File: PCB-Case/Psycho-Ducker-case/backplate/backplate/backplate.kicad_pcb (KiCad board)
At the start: 2 copper layers, 310.6 x 124.2 mm, 0 parts

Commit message: fix: backplate filling
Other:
- board size 310.6 x 124.2 mm -> 310 x 124 mm

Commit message: feat: backplate now has mounting holes compatible with the main pcb
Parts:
- added G***: LOGO, LOGO, F.Cu at (215.0, 141.0)
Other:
- outline, holes or cut-outs redrawn

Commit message: feat: changed backplate pattern
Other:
- outline, holes or cut-outs redrawn
- board text added: "NB: to be flipped, the holes are in reference to the front of the pcb"

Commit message: feat: added rubber feet placement
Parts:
- added G***: LOGO, LOGO, B.Cu at (200.0, 139.0)
- G***: moved to B.Cu
- moved G*** 2.00 mm to (215.0, 143.0), turned to 180 degrees
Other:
- outline, holes or cut-outs redrawn
- board text removed: "NB: to be flipped, the holes are in reference to the front of the pcb"

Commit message: feat: added _style_ to the pcb
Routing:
- net (no net): track 0.00 -> 8970.7 mm
- added copper zone on F.Cu, net (none)
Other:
- outline, holes or cut-outs redrawn

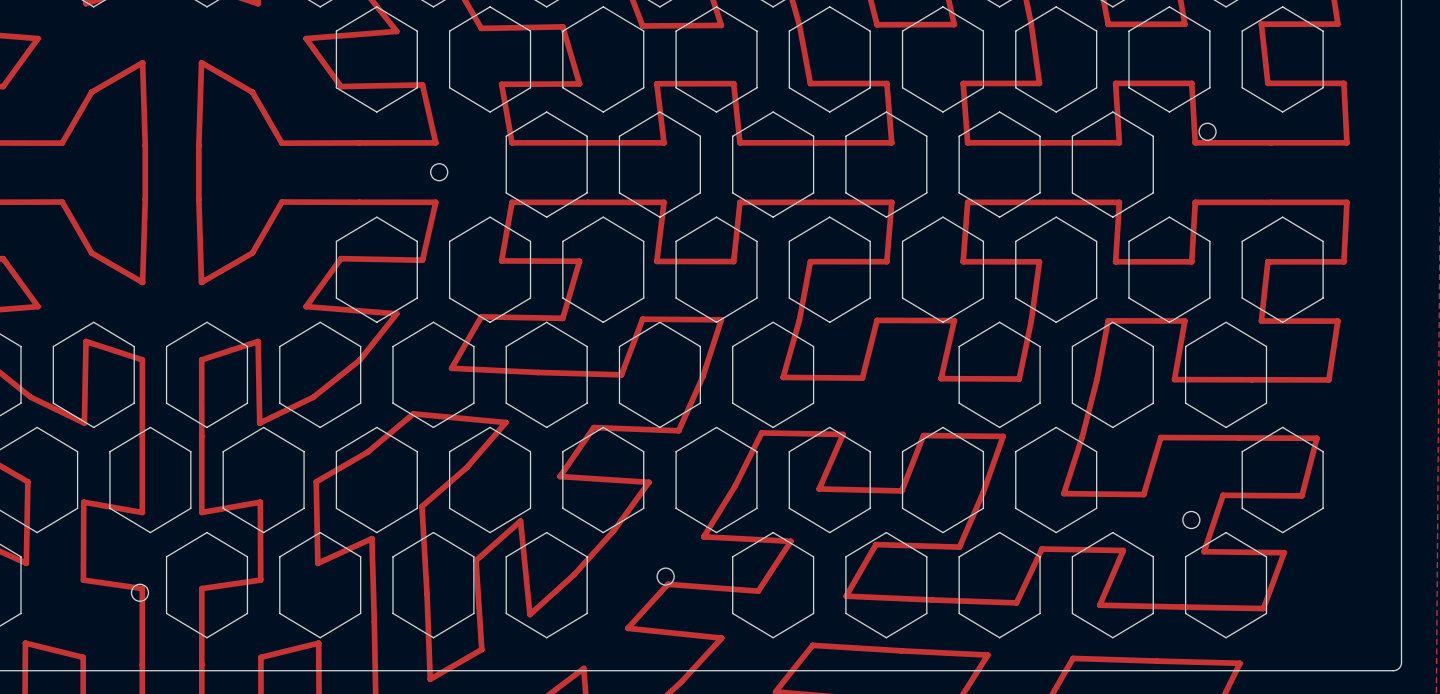
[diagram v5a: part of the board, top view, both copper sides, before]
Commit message: feat: added Bo Burnham cit
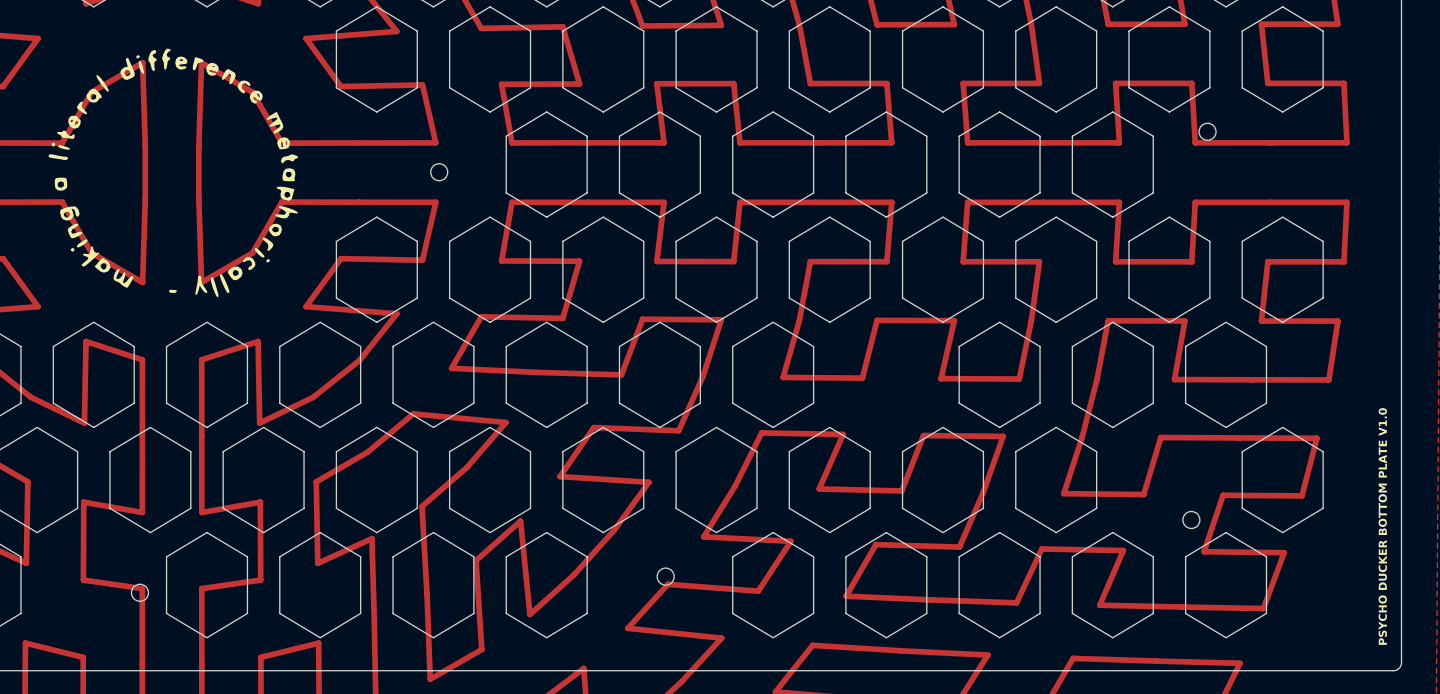
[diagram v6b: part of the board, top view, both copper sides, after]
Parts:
- added G***: LOGO, LOGO, F.Cu at (215.0, 145.0)
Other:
- board text added: "PSYCHO DUCKER BOTTOM PLATE V1.0"

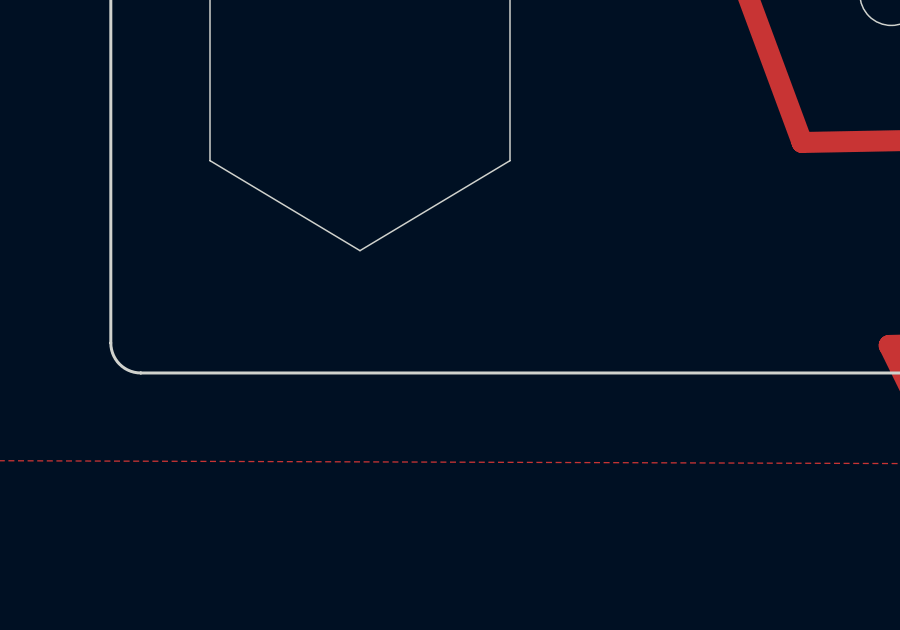
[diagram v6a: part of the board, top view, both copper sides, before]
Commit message: feat: added JLC PCB required text
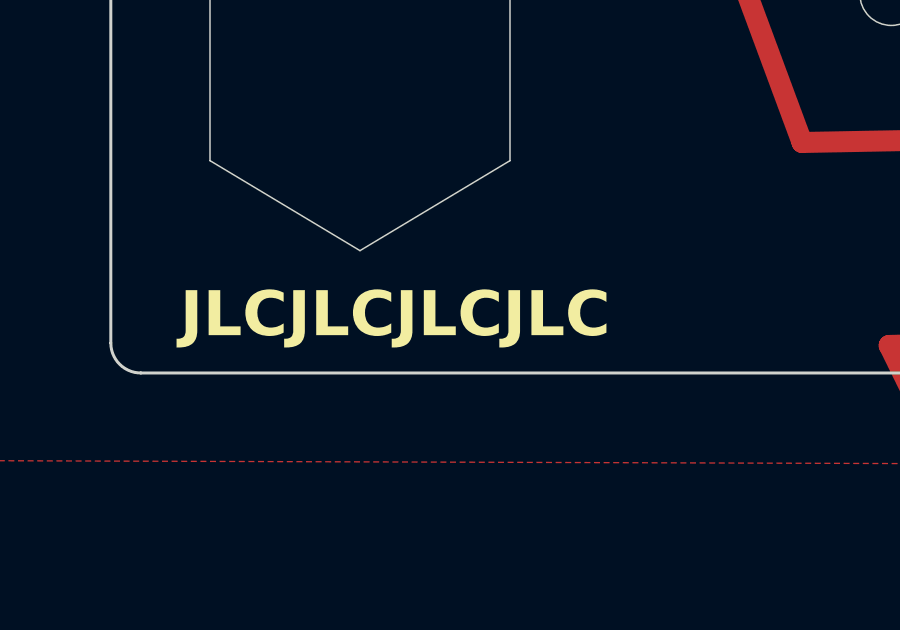
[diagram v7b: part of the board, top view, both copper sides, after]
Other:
- board text added: "JLCJLCJLCJLC"
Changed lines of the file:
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@@
 		(layer "Edge.Cuts")
+	)
+	(gr_text "JLCJLCJLCJLC"
+		(at 59 205 0)
+		(layer "F.SilkS")
+		(effects
+			(font
+				(size 1.5 1.5)
+				(thickness 0.3)
+				(bold yes)
+			)
+			(justify left bottom)
+		)
 	)
 	(gr_text "PSYCHO DUCKER BOTTOM PLATE V1.0\n"
